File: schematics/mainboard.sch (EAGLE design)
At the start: 145 parts, among them IC1 TEENSY 3.6, IC10 UDN2981A, IC2 LM393, IC3 DRV8835, IC4 LM2596S-ADJ, IC5 LM2596S-5.0, IC6 PCF8574P, IC7 PCF8574P, IC8 LD1117A, IC9 TSOP34830, J1 Servo_1, J10 Uart_5, J11 Servo_3, J12 USB_Host, J13 BNO055, J14 I2C_0 / Uart_3, J15 SPI_1, J16 SPI_2, J17 Uart_6, J18 Maus_select, J19 Erw_analog, J2 Servo_2, J20 Erw_PWM, J21 Erw_GPIO, J23 Uart_1, J24 I2C_3, J3 Erw_Pow, J30 H-Bridge Mode, J4 Uart_2, J5 BPS, J6 Erw_ENA, J7 I2C_2, J8 I2C_Display, J9 RPI_SPI0, Q2 IRL3103, SW1 TL36WO, U1 CNY70, U2 BLE-HM-10, U3 BSS138, U4 BSS138, U5 BSS138, X1 Bat

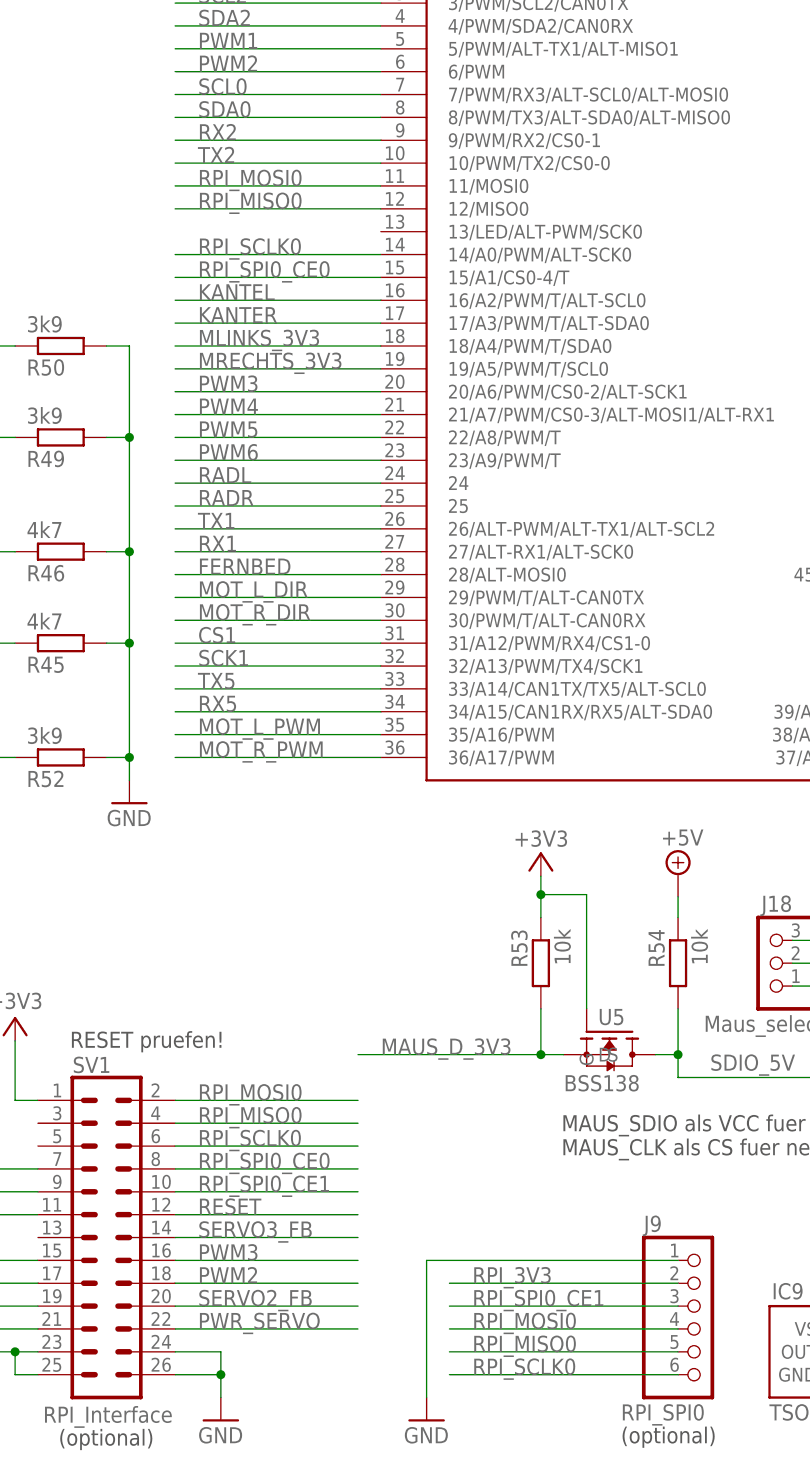
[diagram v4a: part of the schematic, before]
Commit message: mainboard: signal names updated
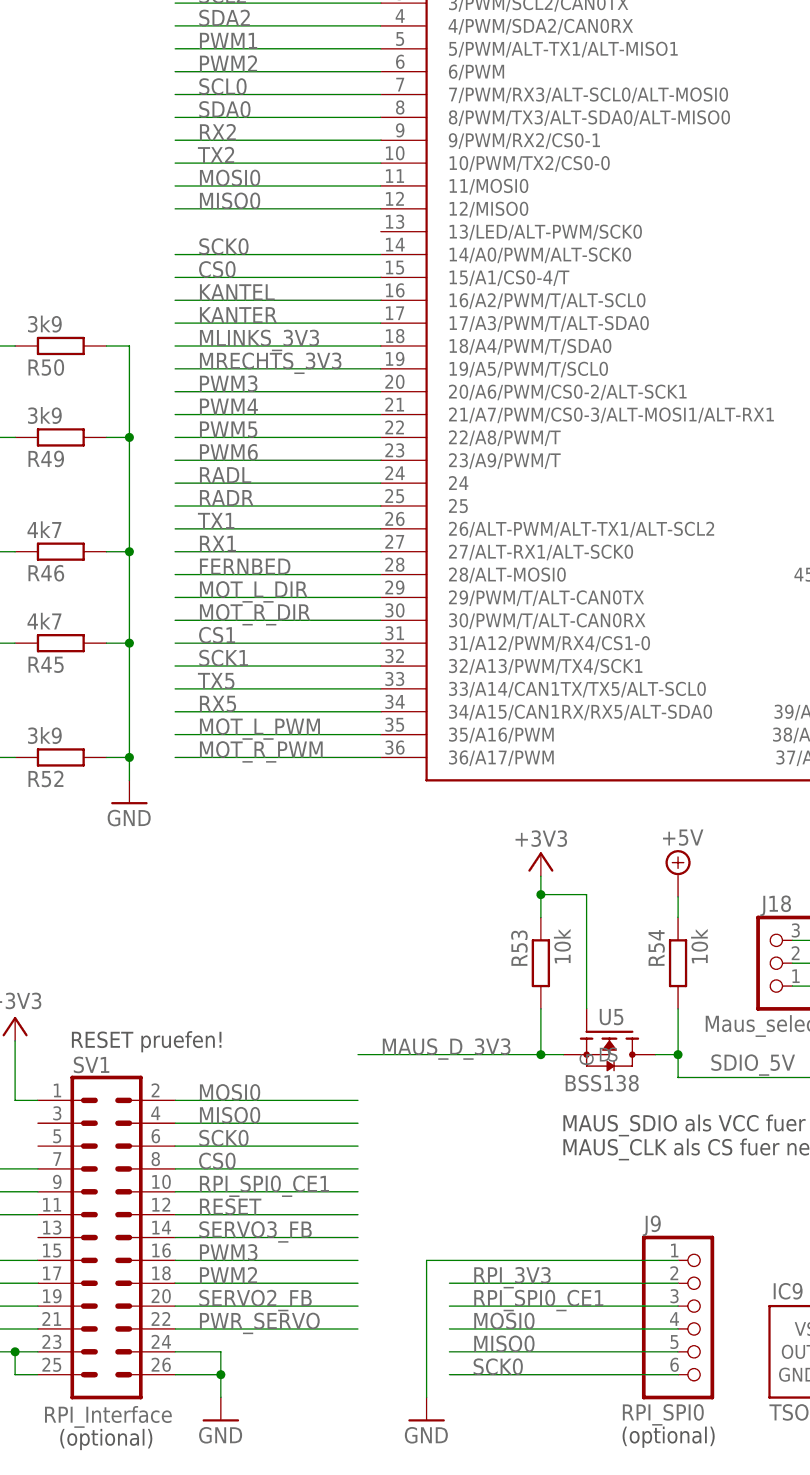
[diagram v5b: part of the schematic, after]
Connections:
- net RPI_MISO0 renamed MISO0
- net RPI_MOSI0 renamed MOSI0
- net RPI_SCLK0 renamed SCK0
- net RPI_SPI0_CE0 renamed CS0
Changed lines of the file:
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@@
 </segment>
 </net>
-<net name="RPI_SPI0_CE0" class="0">
+<net name="CS0" class="0">
 <segment>
 <wire x1="73.66" y1="33.02" x2="53.34" y2="33.02" width="0.1524" layer="91"/>
@@
 </segment>
 </net>
-<net name="RPI_SCLK0" class="0">
+<net name="SCK0" class="0">
 <segment>
 <wire x1="73.66" y1="35.56" x2="53.34" y2="35.56" width="0.1524" layer="91"/>
@@
 </segment>
 </net>
-<net name="RPI_MISO0" class="0">
+<net name="MISO0" class="0">
 <segment>
 <wire x1="73.66" y1="38.1" x2="53.34" y2="38.1" width="0.1524" layer="91"/>
@@
 </segment>
 </net>
-<net name="RPI_MOSI0" class="0">
+<net name="MOSI0" class="0">
 <segment>
 <wire x1="73.66" y1="40.64" x2="53.34" y2="40.64" width="0.1524" layer="91"/>
